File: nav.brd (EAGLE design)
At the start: 160 x 100 mm, 69 parts, among them IC1 FT230XQ, SW1 DHT-4235A, U2 ATMEGA2560-16AU100A-M, U3 MPL3115A2, U4 433MHz, Y1 16MHz

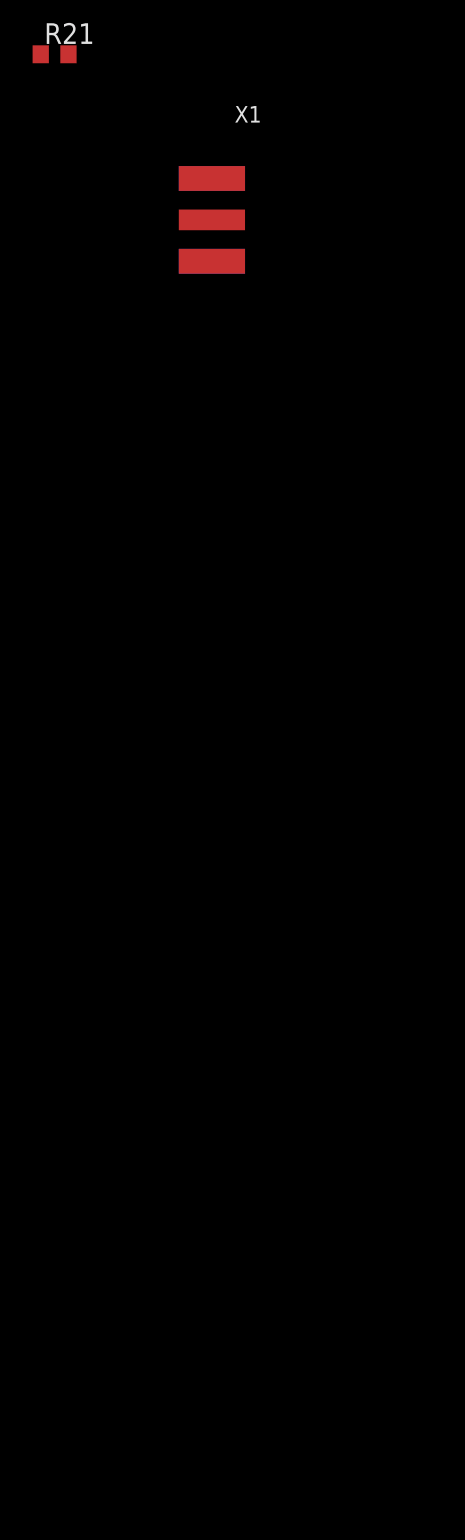
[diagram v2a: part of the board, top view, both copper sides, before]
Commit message: Added Connectors for HC-SR04, UART3 and I2C
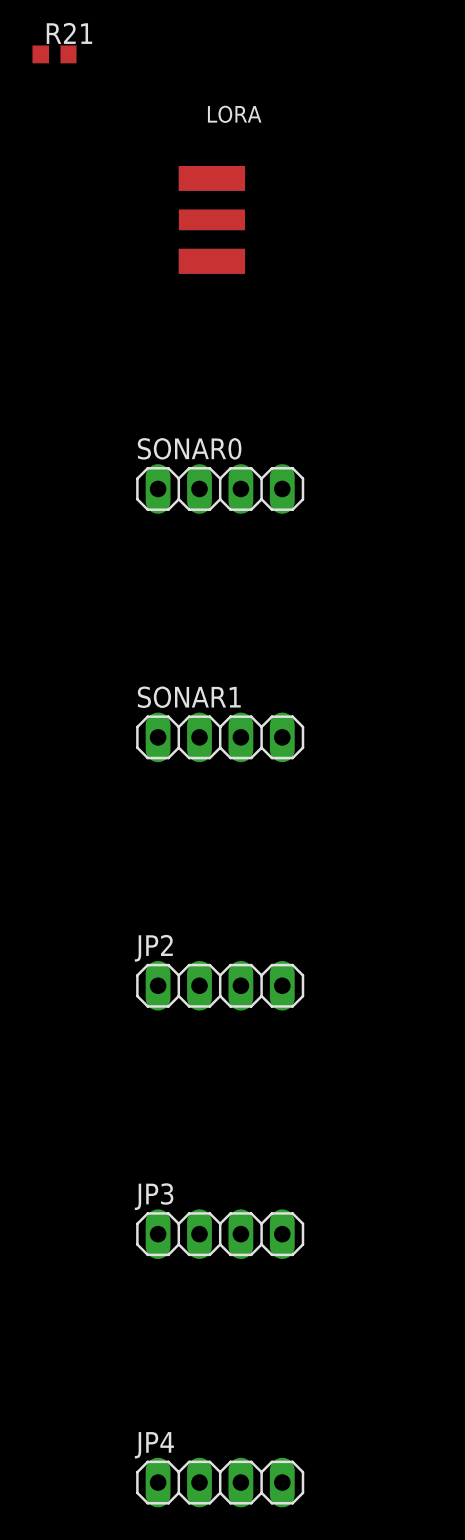
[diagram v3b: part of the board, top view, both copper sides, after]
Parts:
- added JP2, JP3, JP4, SONAR0, SONAR1: (no value), pinhead:1X04
- renumbered X1 to LORA
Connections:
- new net SCL_5V: JP3.3, JP4.3
- new net SDA_5V: JP3.2, JP4.2
- new net SONAR0_ECHO_3V3: U2.85
- new net SONAR0_ECHO_5V: SONAR0.3
- new net SONAR0_TRIGGER_3V3: U2.38
- new net SONAR0_TRIGGER_5V: SONAR0.2
- new net SONAR1_ECHO_3V3: U2.84
- new net SONAR1_ECHO_5V: SONAR1.3
- new net SONAR1_TRIGGER_3V3: U2.39
- new net SONAR1_TRIGGER_5V: SONAR1.2
- new net UART3_RX_5V: JP2.3
- new net UART3_TX_5V: JP2.2
- net +5V: now also JP2.1, JP3.1, JP4.1, SONAR0.1, SONAR1.1
- net GND: now also JP2.4, JP3.4, JP4.4, SONAR0.4, SONAR1.4
- net LED3: now also U2.87; no longer U2.38
- net LED4: now also U2.86; no longer U2.39
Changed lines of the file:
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@@
 </element>
 <element name="R21" library="resistor" library_urn="urn:adsk.eagle:library:348" package="R0603" package3d_urn="urn:adsk.eagle:package:23555/2" value="" x="-5.08" y="-281.94"/>
-<element name="X1" library="adafruit" library_urn="urn:adsk.eagle:library:420" package="SMA_EDGELAUNCH" value="" x="2.54" y="-292.1"/>
+<element name="LORA" library="adafruit" library_urn="urn:adsk.eagle:library:420" package="SMA_EDGELAUNCH" value="" x="2.54" y="-292.1"/>
+<element name="SONAR0" library="pinhead" library_urn="urn:adsk.eagle:library:325" package="1X04" package3d_urn="urn:adsk.eagle:package:22407/2" value="" x="5.08" y="-308.61"/>
+<element name="SONAR1" library="pinhead" library_urn="urn:adsk.eagle:library:325" package="1X04" package3d_urn="urn:adsk.eagle:package:22407/2" value="" x="5.08" y="-323.85"/>
+<element name="JP2" library="pinhead" library_urn="urn:adsk.eagle:library:325" package="1X04" package3d_urn="urn:adsk.eagle:package:22407/2" value="" x="5.08" y="-339.09"/>
+<element name="JP3" library="pinhead" library_urn="urn:adsk.eagle:library:325" package="1X04" package3d_urn="urn:adsk.eagle:package:22407/2" value="" x="5.08" y="-354.33"/>
+<element name="JP4" library="pinhead" library_urn="urn:adsk.eagle:library:325" package="1X04" package3d_urn="urn:adsk.eagle:package:22407/2" value="" x="5.08" y="-369.57"/>
 </elements>
 <signals>
@@
 <contactref element="U4" pad="10"/>
 <contactref element="U4" pad="1"/>
-<contactref element="X1" pad="GND@4"/>
-<contactref element="X1" pad="GND@3"/>
-<contactref element="X1" pad="GND@2"/>
-<contactref element="X1" pad="GND@1"/>
+<contactref element="LORA" pad="GND@4"/>
+<contactref element="LORA" pad="GND@3"/>
+<contactref element="LORA" pad="GND@2"/>
+<contactref element="LORA" pad="GND@1"/>
+<contactref element="SONAR1" pad="4"/>
+<contactref element="SONAR0" pad="4"/>
+<contactref element="JP3" pad="4"/>
+<contactref element="JP4" pad="4"/>
+<contactref element="JP2" pad="4"/>
 <wire x1="-2.96" y1="-243.84" x2="-2.96" y2="-247.65" width="0" layer="19" extent="1-1"/>
 <wire x1="-2.96" y1="-240.03" x2="-2.96" y2="-243.84" width="0" layer="19" extent="1-1"/>
@@
 <wire x1="4.572" y1="-294.64" x2="4.572" y2="-289.56" width="0" layer="19" extent="16-16"/>
 <wire x1="4.572" y1="-294.64" x2="4.572" y2="-294.64" width="0" layer="19" extent="1-16"/>
+<wire x1="8.89" y1="-308.61" x2="4.572" y2="-294.64" width="0" layer="19" extent="16-16"/>
 <wire x1="13.85" y1="-274.24" x2="-1.15" y2="-276.24" width="0" layer="19" extent="1-1"/>
+<wire x1="8.89" y1="-323.85" x2="8.89" y2="-308.61" width="0" layer="19" extent="1-1"/>
+<wire x1="8.89" y1="-339.09" x2="8.89" y2="-323.85" width="0" layer="19" extent="1-1"/>
+<wire x1="8.89" y1="-354.33" x2="8.89" y2="-339.09" width="0" layer="19" extent="1-1"/>
+<wire x1="8.89" y1="-369.57" x2="8.89" y2="-354.33" width="0" layer="19" extent="1-1"/>
 <wire x1="4.572" y1="-212.09" x2="-2.96" y2="-231.14" width="0" layer="19" extent="1-1"/>
 <wire x1="4.572" y1="-212.09" x2="4.572" y2="-212.09" width="0" layer="19" extent="1-16"/>
@@
 </signal>
 <signal name="LED3">
-<contactref element="U2" pad="38"/>
 <contactref element="R12" pad="2"/>
-<wire x1="11.43" y1="-17.9578" x2="31.33" y2="-168.91" width="0" layer="19" extent="1-1"/>
+<contactref element="U2" pad="87"/>
+<wire x1="11.93" y1="-2.3622" x2="31.33" y2="-168.91" width="0" layer="19" extent="1-1"/>
 </signal>
 <signal name="LED4">
-<contactref element="U2" pad="39"/>
 <contactref element="R16" pad="2"/>
-<wire x1="11.93" y1="-17.9578" x2="46.57" y2="-168.91" width="0" layer="19" extent="1-1"/>
+<contactref element="U2" pad="86"/>
+<wire x1="12.43" y1="-2.3622" x2="46.57" y2="-168.91" width="0" layer="19" extent="1-1"/>
 </signal>
 <signal name="LED5">
@@
 <contactref element="PPM7" pad="2"/>
 <contactref element="JP1" pad="2"/>
+<contactref element="SONAR1" pad="1"/>
+<contactref element="SONAR0" pad="1"/>
+<contactref element="JP3" pad="1"/>
+<contactref element="JP4" pad="1"/>
+<contactref element="JP2" pad="1"/>
 <wire x1="10.16" y1="-143.51" x2="10.16" y2="-158.75" width="0" layer="19" extent="1-1"/>
 <wire x1="10.16" y1="-128.27" x2="10.16" y2="-143.51" width="0" layer="19" extent="1-1"/>
@@
 <wire x1="30.48" y1="-113.03" x2="30.48" y2="-128.27" width="0" layer="19" extent="1-1"/>
 <wire x1="30.48" y1="-97.79" x2="30.48" y2="-113.03" width="0" layer="19" extent="1-1"/>
+<wire x1="1.27" y1="-308.61" x2="10.16" y2="-158.75" width="0" layer="19" extent="1-1"/>
+<wire x1="1.27" y1="-323.85" x2="1.27" y2="-308.61" width="0" layer="19" extent="1-1"/>
+<wire x1="1.27" y1="-339.09" x2="1.27" y2="-323.85" width="0" layer="19" extent="1-1"/>
+<wire x1="1.27" y1="-354.33" x2="1.27" y2="-339.09" width="0" layer="19" extent="1-1"/>
+<wire x1="1.27" y1="-369.57" x2="1.27" y2="-354.33" width="0" layer="19" extent="1-1"/>
 </signal>
 <signal name="N$31">
@@
 <signal name="N$30">
 <contactref element="U4" pad="9"/>
-<contactref element="X1" pad="P"/>
+<contactref element="LORA" pad="P"/>
 <wire x1="13.85" y1="-276.24" x2="4.572" y2="-292.1" width="0" layer="19" extent="1-1"/>
 </signal>
@@
 <wire x1="19.2278" y1="-7.16" x2="-1.15" y2="-272.24" width="0" layer="19" extent="1-1"/>
 </signal>
+<signal name="SONAR1_TRIGGER_5V">
+<contactref element="SONAR1" pad="2"/>
+</signal>
+<signal name="SONAR1_ECHO_5V">
+<contactref element="SONAR1" pad="3"/>
+</signal>
+<signal name="SONAR0_TRIGGER_5V">
+<contactref element="SONAR0" pad="2"/>
+</signal>
+<signal name="SONAR0_ECHO_5V">
+<contactref element="SONAR0" pad="3"/>
+</signal>
+<signal name="SONAR0_TRIGGER_3V3">
+<contactref element="U2" pad="38"/>
+</signal>
+<signal name="SONAR1_TRIGGER_3V3">
+<contactref element="U2" pad="39"/>
+</signal>
+<signal name="SONAR0_ECHO_3V3">
+<contactref element="U2" pad="85"/>
+</signal>
+<signal name="SONAR1_ECHO_3V3">
+<contactref element="U2" pad="84"/>
+</signal>
+<signal name="UART3_TX_5V">
+<contactref element="JP2" pad="2"/>
+</signal>
+<signal name="UART3_RX_5V">
+<contactref element="JP2" pad="3"/>
+</signal>
+<signal name="SDA_5V">
+<contactref element="JP3" pad="2"/>
+<contactref element="JP4" pad="2"/>
+<wire x1="3.81" y1="-354.33" x2="3.81" y2="-369.57" width="0" layer="19" extent="1-1"/>
+</signal>
+<signal name="SCL_5V">
+<contactref element="JP3" pad="3"/>
+<contactref element="JP4" pad="3"/>
+<wire x1="6.35" y1="-354.33" x2="6.35" y2="-369.57" width="0" layer="19" extent="1-1"/>
+</signal>
 </signals>

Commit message: First draft of the layout finished
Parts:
- removed JP1, PPM4, PPM5, PPM6, PPM7: (no value), pinhead:1X03
- removed JP2, JP3, JP4: (no value), pinhead:1X04
- removed SW1: DHT-4235A, Seeed-Switch:SW4-SMD-4.2X3.2X2.5MM
- added I2C_0, I2C_1, UART2: (no value), pinhead:1X04
- added POWER: (no value), pinhead:1X03
- added R22, R23: 10k, resistor:R0603
- added RESET: DHT-4235A, Seeed-Switch:SW4-SMD-4.2X3.2X2.5MM
- added U5, U6: (no value), adafruit:TSSOP14
- moved SONAR1 349.5 mm to (19.1, 25.4), turned to 90 degrees
- moved LORA 344.0 mm to (29.5, 50.8), turned to 270 degrees
- moved SONAR0 334.1 mm to (14.0, 25.4), turned to 90 degrees
- moved R21 329.0 mm to (34.5, 44.7), turned to 270 degrees
- moved U4 314.6 mm to (45.2, 42.9), turned to 270 degrees
- moved R20 289.8 mm to (21.6, 30.7), flipped to the bottom, turned to 90 degrees
- moved R14 284.9 mm to (23.9, 30.7), flipped to the bottom, turned to 90 degrees
- moved C5 268.6 mm to (3.81, 20.8), turned to 180 degrees
- moved C4 267.1 mm to (3.81, 23.1), turned to 180 degrees
- moved C2 266.3 mm to (36.8, 28.2), turned to 180 degrees
- moved C3 265.8 mm to (3.81, 25.7), turned to 180 degrees
- moved C1 260.0 mm to (36.8, 25.7), turned to 180 degrees
- moved LED_GPS 254.2 mm to (27.9, 24.9), turned to 270 degrees
- moved R2 248.5 mm to (31.0, 24.9), turned to 180 degrees
- moved R1 228.6 mm to (33.8, 25.9), turned to 90 degrees
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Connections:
- removed net PPM4: PPM4.1, U2.6
- removed net PPM5: PPM5.1, U2.7
- removed net PPM6: PPM6.1, U2.15
- removed net PPM7: PPM7.1, U2.16
- removed net UART3_RX_5V: JP2.3
- removed net UART3_TX_5V: JP2.2
- new net N$36: R23.1, U6.8
- new net N$37: R22.1, U5.8
- new net UART2_RX: U2.12, U5.2
- new net UART2_RX_5V: U5.13, UART2.3
- new net UART2_TX: U2.13, U5.3
- new net UART2_TX_5V: U5.12, UART2.2
- net !RESET: now also RESET.1, RESET.2; no longer SW1.1, SW1.2
- net +3V3: now also U5.1, U6.1
- net +5V: now also I2C_0.1, I2C_1.1, POWER.2, R22.2, R23.2, U5.14, U6.14, UART2.1; no longer JP1.2, JP2.1, JP3.1, JP4.1, PPM4.2, PPM5.2, PPM6.2, PPM7.2
- net GND: now also I2C_0.4, I2C_1.4, POWER.1, POWER.3, RESET.3, RESET.4, U5.7, U6.7, UART2.4; no longer JP1.1, JP1.3, JP2.4, JP3.4, JP4.4, PPM4.3, PPM5.3, PPM6.3, PPM7.3, SW1.3, SW1.4
- net SCL: now also U5.5
- net SCL_5V: now also I2C_0.3, I2C_1.3, U5.10; no longer JP3.3, JP4.3
- net SDA: now also U5.4
- net SDA_5V: now also I2C_0.2, I2C_1.2, U5.11; no longer JP3.2, JP4.2
- net SONAR0_ECHO_3V3: now also U6.2
- net SONAR0_ECHO_5V: now also U6.13
- net SONAR0_TRIGGER_3V3: now also U6.3
- net SONAR0_TRIGGER_5V: now also U6.12
- net SONAR1_ECHO_3V3: now also U6.4
- net SONAR1_ECHO_5V: now also U6.11
- net SONAR1_TRIGGER_3V3: now also U6.5
- net SONAR1_TRIGGER_5V: now also U6.10
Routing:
- net +3V3: track 0.00 -> 211.5 mm, vias 0 -> 16
- net +5V: track 0.00 -> 95.1 mm, vias 0 -> 1
- net MISO: track 0.00 -> 83.0 mm, vias 0 -> 1
- net MOSI: track 0.00 -> 80.3 mm, vias 0 -> 1
- net SCK: track 0.00 -> 77.2 mm, vias 0 -> 1
- net !RESET: track 0.00 -> 67.0 mm, vias 0 -> 3
- net BARO_INT2: track 0.00 -> 56.8 mm, vias 0 -> 3
- net BARO_INT1: track 0.00 -> 54.2 mm, vias 0 -> 3
- net LED4: track 0.00 -> 47.8 mm, vias 0 -> 3
- net SONAR1_ECHO_3V3: track 0.00 -> 47.8 mm, vias 0 -> 2
- net LED3: track 0.00 -> 44.3 mm, vias 0 -> 3
- net PPM0: track 0.00 -> 43.5 mm, vias 0 -> 5
- net SONAR0_ECHO_3V3: track 0.00 -> 42.9 mm, vias 0 -> 2
- net LED7: track 0.00 -> 41.0 mm, vias 0 -> 1
- net LED5: track 0.00 -> 39.3 mm, vias 0 -> 1
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- added copper zone on layer 1, net GND
- added copper zone on layer 16, net GND
